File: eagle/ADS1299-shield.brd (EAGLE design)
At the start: 101.6 x 53.3 mm, 133 parts, among them IC1 ADS1299IPAG, IC2 TPS72325DBVT, IC3 TPS73225DBVT, IC5 24AA256UID, IC6 TPS604XXDBV, IC7 OPA376DBV, IC8 OPA376DBV, IC9 TXS0102DCTR, J8 Electrode Connector, U2 TXB0108PWR, U3 TXB0108PWR

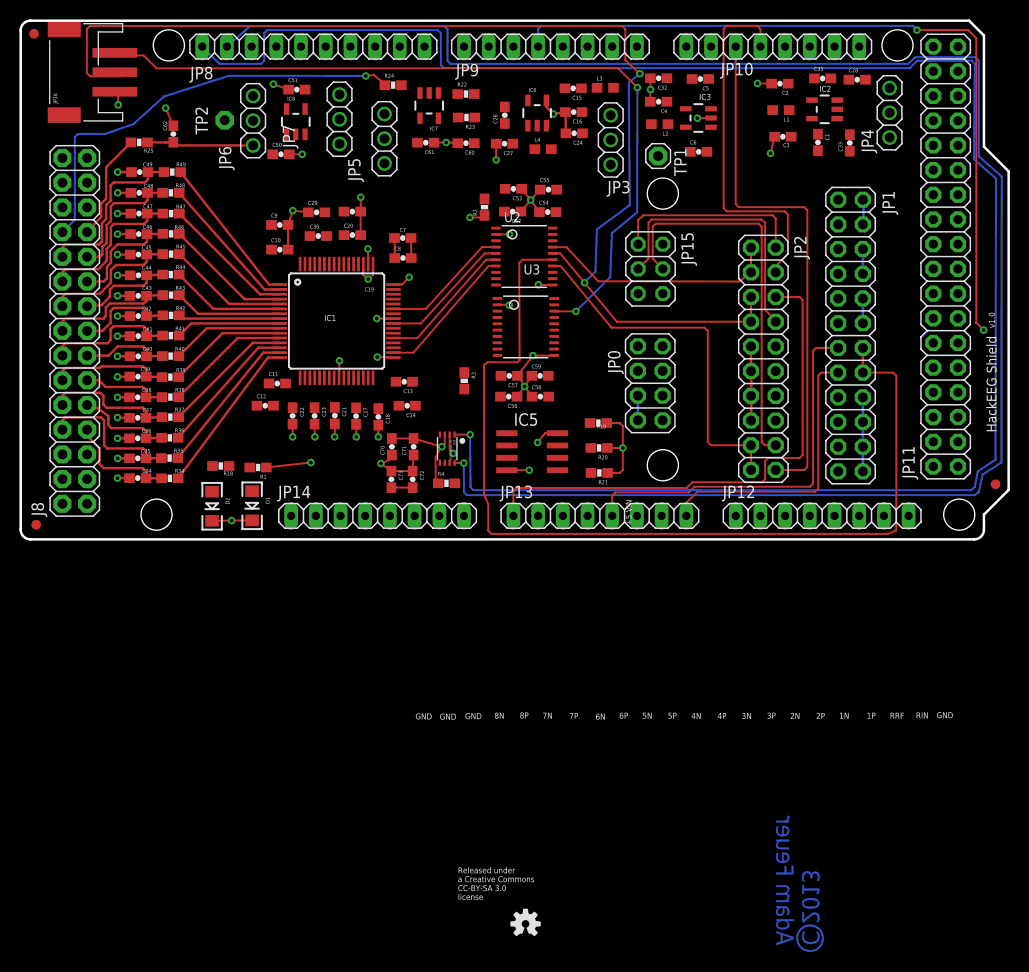
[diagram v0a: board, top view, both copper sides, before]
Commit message: routed CLK output around board edge to avoid power supplies
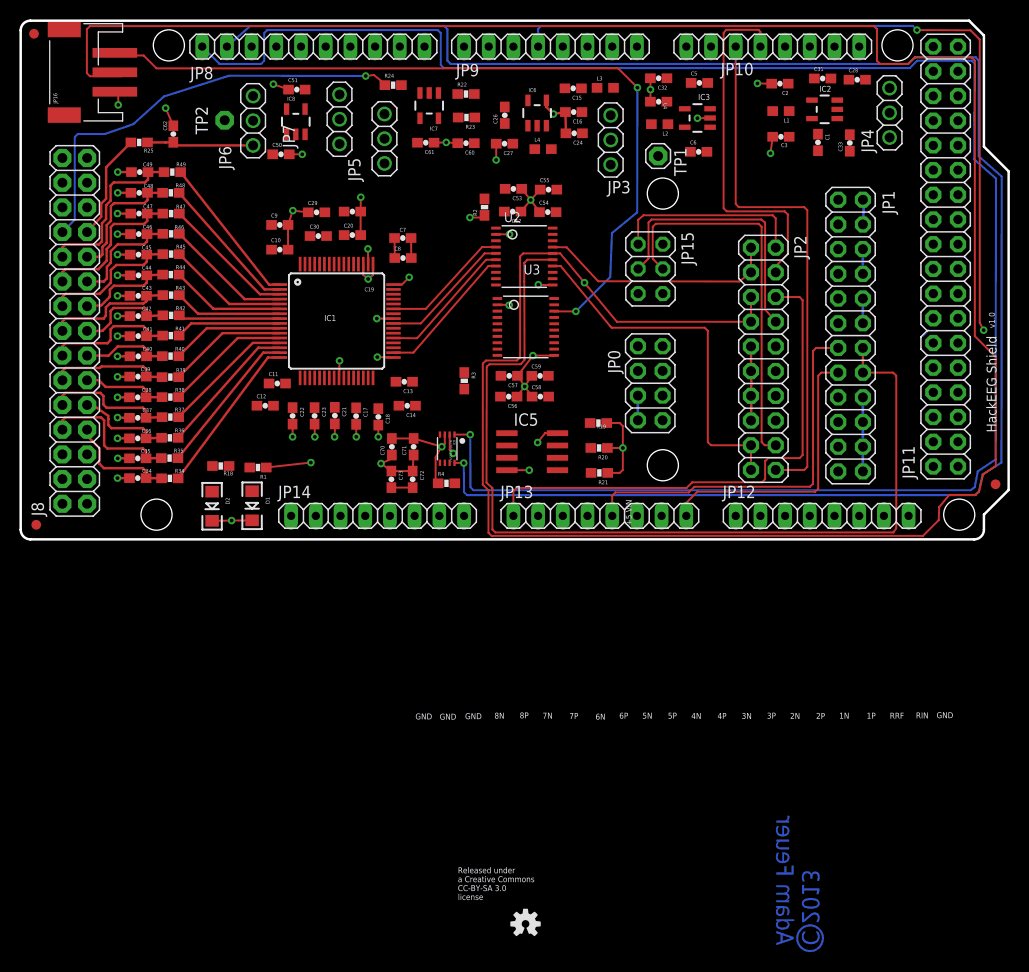
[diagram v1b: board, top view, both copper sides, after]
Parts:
- moved C5 0.42 mm to (69.9, 47.1), turned to 0 degrees
- moved C3 0.20 mm to (78.3, 41.5)
- moved IC3 0.10 mm to (69.7, 43.5)
- moved L1 0.10 mm to (78.3, 44.2)
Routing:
- net ADS_SPI_CLK: track 120.4 -> 265.5 mm, vias 2 -> 1
- net ADS_CLK: track 98.7 -> 97.9 mm
- net USART1_MISO: track 37.6 -> 36.9 mm

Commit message: configuration jumper section completely routed
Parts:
- moved JP7 10.8 mm to (23.2, 38.7), turned to 0 degrees
- moved C50 4.20 mm to (31.1, 40.2), turned to 180 degrees
- moved C22 3.56 mm to (28.3, 9.27)
- moved TP2 3.56 mm to (24.0, 45.4)
- moved C12 3.03 mm to (27.6, 11.9)
- moved IC8 2.54 mm to (31.0, 43.2), turned to 270 degrees
- moved C11 2.41 mm to (27.6, 14.0)
- moved JP6 1.29 mm to (23.1, 42.3), turned to 0 degrees
- moved JP5 1.29 mm to (36.3, 40.9)
- moved C51 0.74 mm to (29.2, 46.2)
- moved JP1 0.51 mm to (88.0, 20.3)
- moved C13 0.43 mm to (39.9, 16.0)
- moved R24 0.42 mm to (38.5, 46.4)
- moved JP2 0.38 mm to (76.5, 19.1)
- moved C31 0.29 mm to (82.7, 47.2)
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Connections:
- new net N$570: JP14.5
- new net N$571: JP11.1
- new net N$572: JP11.2
- net VCC_5V: no longer JP11.1, JP11.2, JP14.5
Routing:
- net !ADC_CS_1: track 0.00 -> 108.0 mm, vias 0 -> 3
- net !ADC_CS_2: track 0.00 -> 58.4 mm
- net AGND: track 355.5 -> 402.6 mm, vias 47 -> 51
- net ADS_DRDY: track 7.62 -> 51.3 mm, vias 0 -> 1
- net !ADS_PWDN: track 2.67 -> 45.4 mm, vias 0 -> 1
- net !ADS_RESET: track 2.54 -> 40.1 mm, vias 0 -> 2
- net AVDD: track 2.06 -> 39.5 mm
- net !ADC_PWDN_0: track 0.00 -> 34.3 mm, vias 0 -> 2
- net SRB2: track 0.00 -> 32.6 mm, vias 0 -> 1
- net !ADC_RESET_0: track 0.00 -> 30.9 mm, vias 0 -> 1
- net !ADC_CS_3: track 0.00 -> 29.9 mm
- net ADS_START: track 85.7 -> 115.6 mm, vias 2 -> 3
- net !ADC_PWDN_1: track 0.00 -> 24.4 mm
- net VCC_5V: track 0.00 -> 24.2 mm
- net ADC_START_0: track 0.00 -> 22.6 mm
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
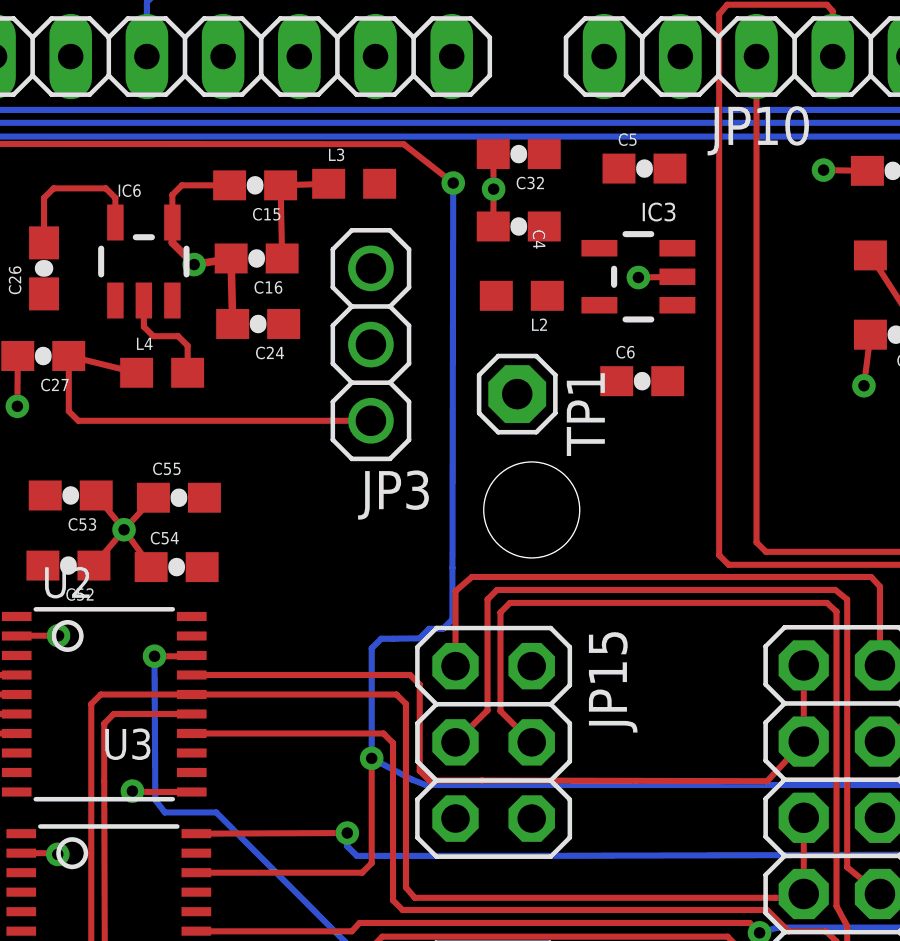
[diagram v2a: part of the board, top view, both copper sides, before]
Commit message: moved VCC_5V trace from DVDD layer to BOTTOM
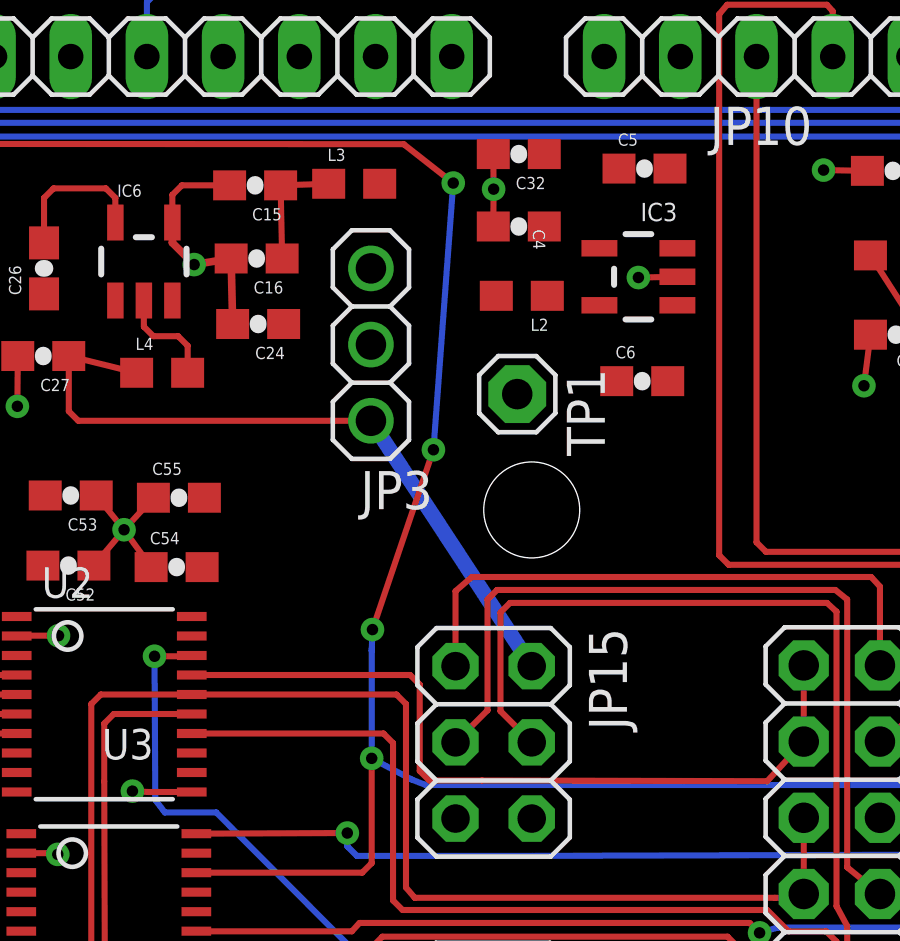
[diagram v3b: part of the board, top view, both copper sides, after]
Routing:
- net ADS_START: track 115.6 -> 113.9 mm, vias 3 -> 5
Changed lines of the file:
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@@
 <contactref element="JP3" pad="1"/>
 <contactref element="JP15" pad="2"/>
-<wire x1="66.167" y1="30.48" x2="60.8076" y2="38.6588" width="0.6096" layer="15"/>
+<wire x1="66.167" y1="30.48" x2="60.8076" y2="38.6588" width="0.508" layer="16"/>
 <wire x1="50.7356" y1="40.8178" x2="50.7356" y2="38.9763" width="0.2032" layer="1"/>
 <wire x1="50.7356" y1="38.9763" x2="51.0531" y2="38.6588" width="0.2032" layer="1"/>
@@
 <wire x1="50.7356" y1="40.8178" x2="52.998" y2="40.259" width="0.2032" layer="1"/>
 <wire x1="71.0231" y1="42.5094" x2="71.0231" y2="44.4094" width="0" layer="19" extent="1-1"/>
-<wire x1="60.8076" y1="38.6588" x2="71.0231" y2="42.5094" width="0" layer="19" extent="1-15"/>
+<wire x1="60.8076" y1="38.6588" x2="71.0231" y2="42.5094" width="0" layer="19" extent="1-16"/>
 </signal>
 <signal name="AIN1P">
@@
 <wire x1="61.8998" y1="47.879" x2="63.5508" y2="46.5836" width="0.2032" layer="1"/>
 <via x="63.5508" y="46.5836" extent="1-16" drill="0.381"/>
-<wire x1="63.5508" y1="46.5836" x2="63.5254" y2="33.7566" width="0.2032" layer="16"/>
-<wire x1="63.5254" y1="33.7566" x2="63.5254" y2="32.0421" width="0.2032" layer="16"/>
-<wire x1="63.5254" y1="32.0421" x2="63.2079" y2="31.7246" width="0.2032" layer="16"/>
-<wire x1="63.2079" y1="31.7246" x2="62.7507" y2="31.7246" width="0.2032" layer="16"/>
-<wire x1="62.7507" y1="31.7246" x2="62.4332" y2="31.4071" width="0.2032" layer="16"/>
+<wire x1="63.5508" y1="46.5836" x2="62.8904" y2="37.6936" width="0.2032" layer="16"/>
 <wire x1="54.9878" y1="23.596" x2="60.5155" y2="23.596" width="0.2032" layer="1"/>
 <wire x1="60.5155" y1="23.596" x2="60.833" y2="23.9135" width="0.2032" layer="1"/>
 <wire x1="60.833" y1="23.9135" x2="60.833" y2="27.4066" width="0.2032" layer="1"/>
 <via x="60.833" y="27.4066" extent="1-16" drill="0.381"/>
-<wire x1="60.833" y1="27.4066" x2="60.833" y2="31.0769" width="0.2032" layer="16"/>
-<wire x1="60.833" y1="31.0769" x2="61.1505" y2="31.3944" width="0.2032" layer="16"/>
-<wire x1="61.1505" y1="31.3944" x2="61.5442" y2="31.3944" width="0.2032" layer="16"/>
-<wire x1="61.5442" y1="31.3944" x2="62.4332" y2="31.4071" width="0.2032" layer="16"/>
+<wire x1="60.833" y1="27.4066" x2="60.833" y2="30.988" width="0.2032" layer="16"/>
+<wire x1="60.833" y1="30.988" x2="60.833" y2="31.0769" width="0.2032" layer="16"/>
 <wire x1="86.741" y1="25.4" x2="85.6488" y2="26.4922" width="0.2032" layer="1"/>
 <wire x1="85.6488" y1="26.4922" x2="83.3628" y2="26.4922" width="0.2032" layer="1"/>
@@
 <wire x1="62.6364" y1="26.5176" x2="62.1792" y2="26.6954" width="0.2032" layer="16"/>
 <wire x1="62.1792" y1="26.6954" x2="60.833" y2="27.4066" width="0.2032" layer="16"/>
+<via x="62.8904" y="37.6936" extent="1-16" drill="0.381"/>
+<wire x1="62.8904" y1="37.6936" x2="60.8584" y2="31.6992" width="0.2032" layer="1"/>
+<via x="60.8584" y="31.6992" extent="1-16" drill="0.381"/>
+<wire x1="60.8584" y1="31.6992" x2="60.833" y2="30.988" width="0.2032" layer="16"/>
 </signal>
 <signal name="N$14">
@@
 <wire x1="13.169" y1="40.9448" x2="15.025" y2="40.9448" width="0.254" layer="1"/>
 <wire x1="15.025" y1="40.9448" x2="15.8242" y2="40.9584" width="0.254" layer="1"/>
-<wire x1="20.574" y1="42.2656" x2="20.6502" y2="38.6842" width="0" layer="19" extent="1-1"/>
+<wire x1="20.6502" y1="38.6842" x2="20.574" y2="42.2656" width="0" layer="19" extent="1-1"/>
 <wire x1="15.8242" y1="40.9584" x2="20.574" y2="42.2656" width="0" layer="19" extent="1-1"/>
 </signal>
@@
 <contactref element="IC8" pad="1"/>
 <contactref element="IC8" pad="4"/>
-<wire x1="32.2627" y1="42.23" x2="25.7302" y2="38.6842" width="0" layer="19" extent="1-1"/>
-<wire x1="29.6625" y1="44.13" x2="32.2627" y2="42.23" width="0" layer="19" extent="1-1"/>
+<wire x1="32.2627" y1="42.23" x2="29.6625" y2="44.13" width="0" layer="19" extent="1-1"/>
+<wire x1="25.7302" y1="38.6842" x2="29.6625" y2="44.13" width="0" layer="19" extent="1-1"/>
 </signal>
 <signal name="N$15">
@@
 <wire x1="45.0431" y1="43.4293" x2="45.124" y2="43.5102" width="0.2032" layer="1"/>
 <wire x1="46.7732" y1="40.8686" x2="85.3186" y2="41.5916" width="0" layer="19" extent="1-1"/>
-<wire x1="40.2708" y1="31.115" x2="46.7732" y2="40.8686" width="0" layer="19" extent="1-1"/>
-<wire x1="34.3636" y1="28.4306" x2="40.2962" y2="29.0576" width="0" layer="19" extent="1-1"/>
-<wire x1="32.3636" y1="28.4306" x2="34.3636" y2="28.4306" width="0" layer="19" extent="1-1"/>
-<wire x1="31.8636" y1="28.4306" x2="32.3636" y2="28.4306" width="0" layer="19" extent="1-1"/>
-<wire x1="31.584" y1="31.3182" x2="31.8636" y2="28.4306" width="0" layer="19" extent="1-1"/>
-<wire x1="31.4062" y1="33.7566" x2="31.584" y2="31.3182" width="0" layer="19" extent="1-1"/>
-<wire x1="31.9142" y1="40.2336" x2="31.4062" y2="33.7566" width="0" layer="19" extent="1-1"/>
-<wire x1="32.2627" y1="44.13" x2="31.9142" y2="40.2336" width="0" layer="19" extent="1-1"/>
+<wire x1="32.2627" y1="44.13" x2="43.0886" y2="43.4293" width="0" layer="19" extent="1-1"/>
+<wire x1="31.9142" y1="40.2336" x2="32.2627" y2="44.13" width="0" layer="19" extent="1-1"/>
+<wire x1="31.4062" y1="33.7566" x2="31.9142" y2="40.2336" width="0" layer="19" extent="1-1"/>
+<wire x1="31.584" y1="31.3182" x2="31.4062" y2="33.7566" width="0" layer="19" extent="1-1"/>
+<wire x1="31.8636" y1="28.4306" x2="31.584" y2="31.3182" width="0" layer="19" extent="1-1"/>
+<wire x1="32.3636" y1="28.4306" x2="31.8636" y2="28.4306" width="0" layer="19" extent="1-1"/>
+<wire x1="34.3636" y1="28.4306" x2="32.3636" y2="28.4306" width="0" layer="19" extent="1-1"/>
+<wire x1="40.2962" y1="29.0576" x2="34.3636" y2="28.4306" width="0" layer="19" extent="1-1"/>
 <wire x1="23.9522" y1="45.3644" x2="32.2627" y2="44.13" width="0" layer="19" extent="1-1"/>
-<wire x1="31.8636" y1="16.7306" x2="32.3636" y2="28.4306" width="0" layer="19" extent="1-1"/>
+<wire x1="31.8636" y1="16.7306" x2="31.8636" y2="28.4306" width="0" layer="19" extent="1-1"/>
 <wire x1="30.3636" y1="16.7306" x2="31.8636" y2="16.7306" width="0" layer="19" extent="1-1"/>
 <wire x1="36.3636" y1="16.7306" x2="31.8636" y2="16.7306" width="0" layer="19" extent="1-1"/>

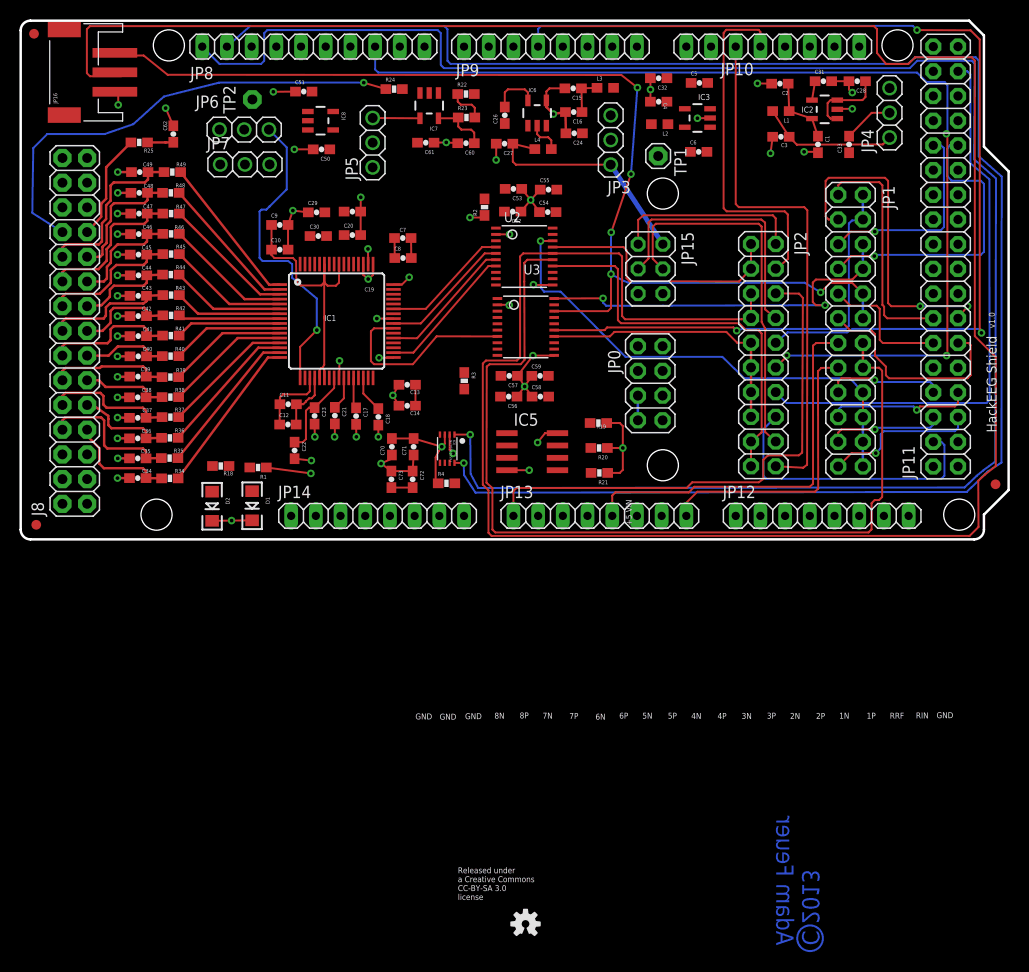
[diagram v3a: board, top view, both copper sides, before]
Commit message: board fully routed - needs cleanup of traces and optimization
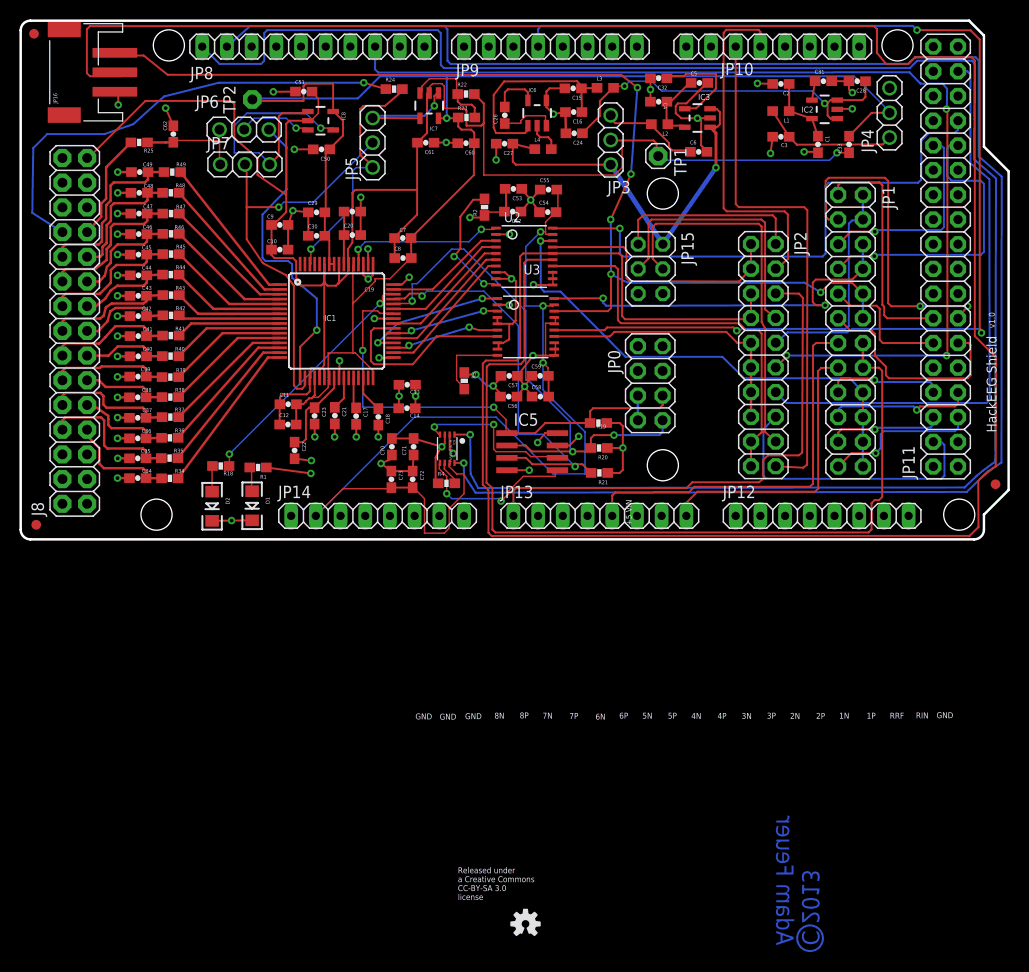
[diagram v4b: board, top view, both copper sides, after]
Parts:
- moved C14 0.26 mm to (39.9, 13.6)
- moved C30 0.18 mm to (30.6, 31.3)
- moved C2 0.10 mm to (78.3, 47.0)
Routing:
- net AVDD: track 39.5 -> 184.9 mm, vias 0 -> 1
- net AVSS: track 19.4 -> 163.8 mm, vias 0 -> 1
- net IOREF: track 2.18 -> 102.5 mm, vias 0 -> 3
- net AGND: track 402.6 -> 466.3 mm, vias 51 -> 53
- net ADS_CLKSEL: track 0.00 -> 57.1 mm, vias 0 -> 1
- net BOARD_ADDR_1: track 0.00 -> 55.4 mm, vias 0 -> 3
- net BOARD_ADDR_0: track 0.00 -> 48.8 mm, vias 0 -> 2
- net SRB1: track 0.00 -> 43.0 mm, vias 0 -> 1
- net BOARD_ADDR_2: track 0.00 -> 42.9 mm, vias 0 -> 2
- net VCC_-5V: track 8.20 -> 37.5 mm, vias 0 -> 2
- net N$17: track 0.00 -> 27.0 mm, vias 0 -> 1
- net BIAS_ELEC: track 0.00 -> 25.5 mm, vias 0 -> 1
- net GPIO4: track 0.00 -> 25.3 mm, vias 0 -> 2
- net N$7: track 4.04 -> 22.4 mm
- net VCC_5V: track 24.2 -> 42.4 mm, vias 0 -> 1
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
